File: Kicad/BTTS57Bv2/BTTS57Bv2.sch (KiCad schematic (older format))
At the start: 70 parts, among them K1-RES SW_Push, K2-Next SW_Push, K3-Mode SW_Push, K4-Valid SW_Push, P1 Conn_01x06, P2 Conn_01x04, P4 Conn_01x08, P5 Conn_01x02, U1 BNOR11, U2 A4950E, U3 EL-0631, U4 A4950E, U5 TLE5012B, U6 EL357NC, U7 STM32F103CBTx, U8 LD1117S33CTR, U9 PCA82C251, Y1 Crystal, p7 Conn_01x08

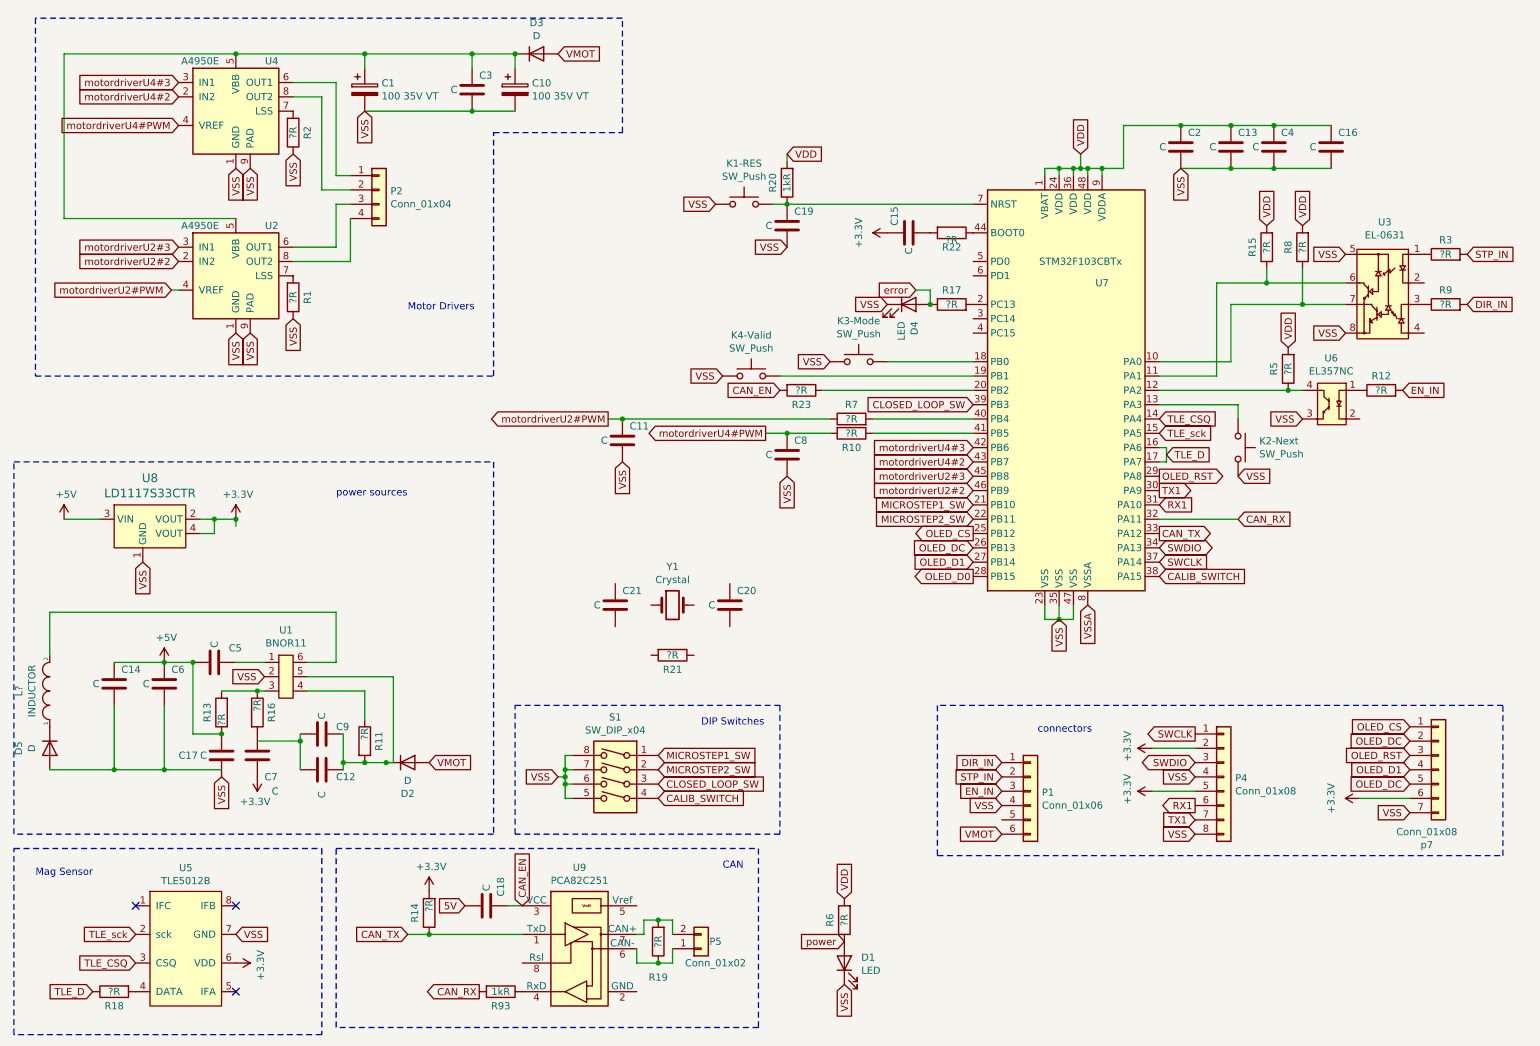
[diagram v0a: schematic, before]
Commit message: fix connection on CAN, add cristal wiring
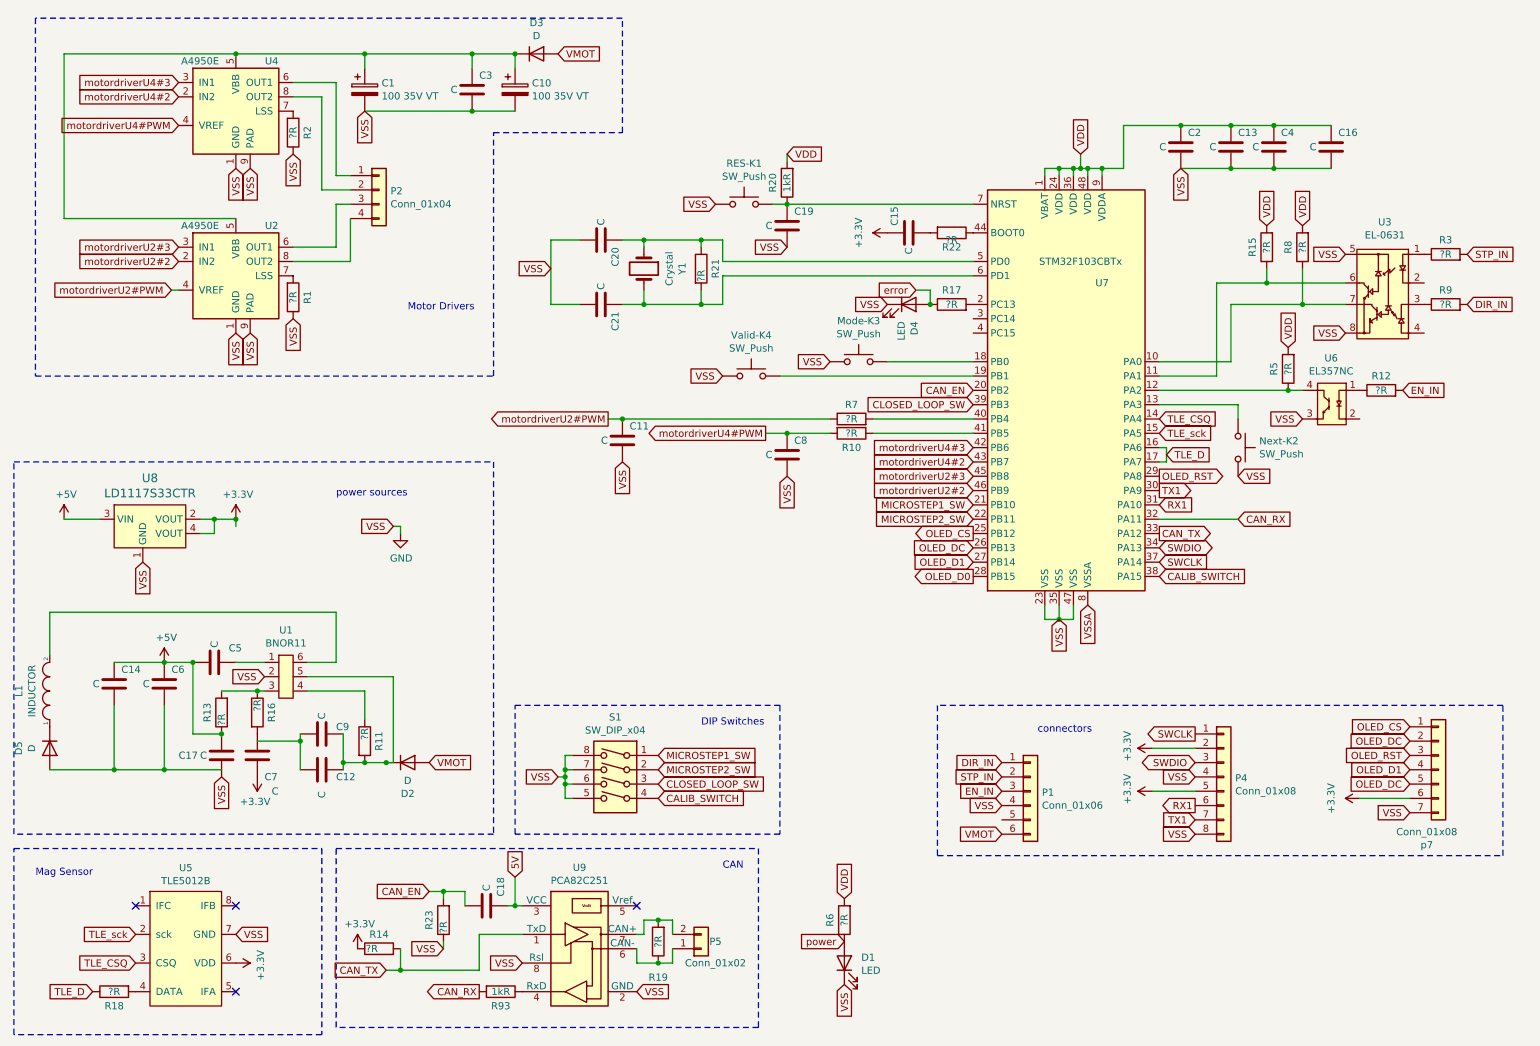
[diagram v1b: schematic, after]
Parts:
- gave numbers to parts that had none: 1
- renumbered K3-Mode to Mode-K3, K2-Next to Next-K2, K1-RES to RES-K1, K4-Valid to Valid-K4
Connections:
- net VSS is gone; now on net GND: C1.2, C10.2, C11.2, C13.2, C16.2, C17.2, C19.2, C2.2, C3.2, C4.2, C8.2, D1.1 (K), D4.1 (K), Mode-K3.1, Next-K2.2, P1.4 (Pin_4), P4.4 (Pin_4), P4.8 (Pin_8), R1.1, R2.1, RES-K1.1, S1.5, S1.6, S1.7, S1.8, U1.2, U2.1 (GND), U2.9 (PAD), U3.5, U3.8, U4.1 (GND), U4.9 (PAD), U5.7 (GND), U6.3, U7.23 (VSS), U7.35 (VSS), U7.47 (VSS), U8.1 (GND), Valid-K4.1, p7.7 (Pin_7)
- net +3V3: now also R14.1; no longer R14.2
- net 5V: now also C18.1, U9.3 (VCC); no longer C18.2
- net CAN_EN: now also C18.2, U7.20 (PB2); no longer C18.1, U9.3 (VCC)
- net CAN_TX: now also R14.2; no longer R14.1
- net GND: now reaches R23.1
- net GND: now also C20.2, C21.2, U9.2 (GND), U9.8 (Rsl); no longer U7.20 (PB2)
- net at U7.5 (PD0): now also C20.1, R21.1, Y1.1
- net at U7.6 (PD1): now also C21.1, R21.2, Y1.2
- no-connect marks 3 -> 4
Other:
- moved on the sheet: C20, C21, R14, R21, R23, Y1

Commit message: added footprint information changed orientation of oled connector added mounting holes PCB reverse creation (high parts are positionned according measurements, same for outline)
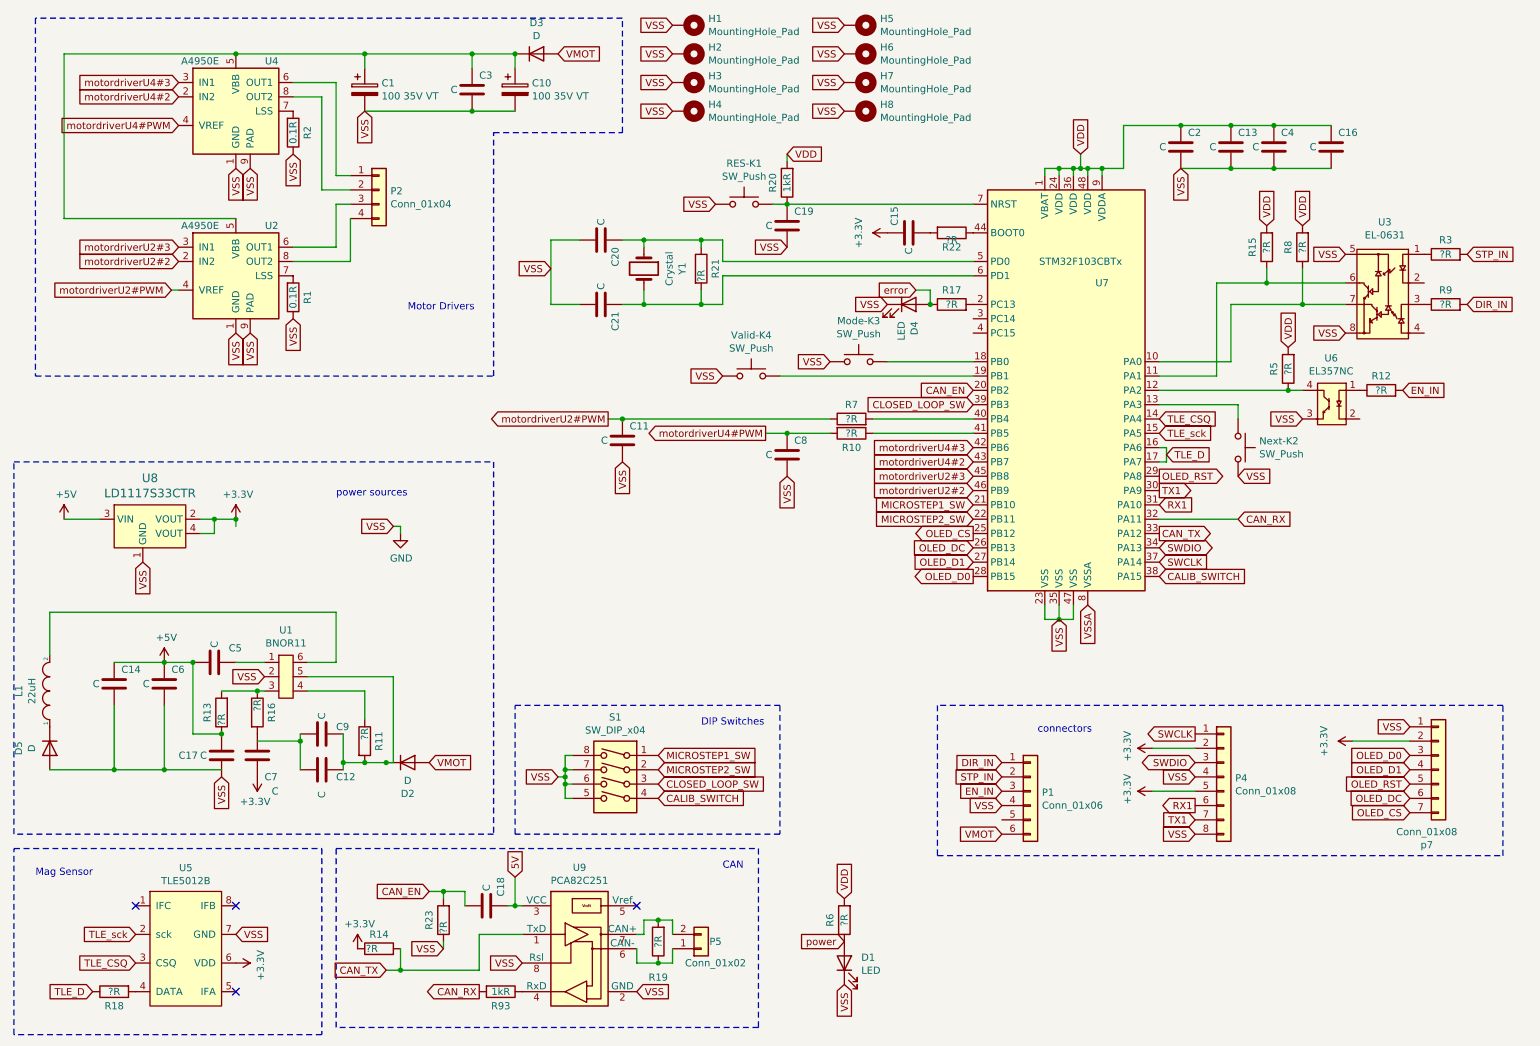
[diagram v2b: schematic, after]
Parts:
- added H1, H2, H3, H4, H5, H6, H7, H8: MountingHole_Pad, MountingHole:MountingHole_2.7mm_M2.5_ISO14580_Pad_TopBottom, symbol Mechanical:MountingHole_Pad
- C1, C10: footprint (none) -> Capacitor_SMD:CP_Elec_6.3x7.7
- C11, C12, C13, C14, C15, C16, C18, C19, C2, C20, C21, C4, C5, C8: footprint (none) -> Capacitor_SMD:C_0603_1608Metric
- C17, C3, C7: footprint (none) -> Capacitor_SMD:C_1812_4532Metric
- C6, C9: footprint (none) -> Capacitor_SMD:C_0805_2012Metric
- D1, D4: footprint (none) -> LED_SMD:LED_0603_1608Metric
- D2, D3, D5: footprint (none) -> Diode_SMD:D_2512_6332Metric
- L1: value INDUCTOR -> 22uH; footprint (none) -> Inductor_SMD:L_Wuerth_MAPI-4030; uncertain (none) -> yes
- Mode-K3, Next-K2, RES-K1, Valid-K4: footprint (none) -> Button_Switch_SMD:SW_Push_1P1T-SH_NO_CK_KMR2xxG
- P2: footprint (none) -> Connector_JST:JST_XH_B4B-XH-A_1x04_P2.50mm_Vertical
- P4: footprint (none) -> Connector_PinHeader_2.54mm:PinHeader_1x08_P2.54mm_Vertical
- R1, R2: value ?R -> 0.1R; footprint (none) -> Resistor_SMD:R_2512_6332Metric
- R10, R11, R13, R14, R15, R16, R17, R20, R21, R22, R23, R5, R6, R7, R8, R93: footprint (none) -> Resistor_SMD:R_0603_1608Metric
- R12, R18, R3, R9: footprint (none) -> Resistor_SMD:R_0805_2012Metric
- R19: footprint (none) -> Resistor_SMD:R_1206_3216Metric
- U3: footprint (none) -> Package_SO:SOP-8_3.9x4.9mm_P1.27mm
- U6: footprint (none) -> Package_SO:SOP-4_3.8x4.1mm_P2.54mm
- p7: footprint (none) -> Connector_PinSocket_2.54mm:PinSocket_1x07_P2.54mm_Vertical
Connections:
- net +3V3: now also p7.2 (Pin_2); no longer p7.6 (Pin_6)
- net GND: now also p7.1 (Pin_1), H1.1, H2.1, H3.1, H4.1, H5.1, H6.1, H7.1, H8.1; no longer p7.7 (Pin_7)
- net OLED_CS: now also p7.7 (Pin_7); no longer p7.1 (Pin_1)
- net OLED_D0: now also p7.3 (Pin_3)
- net OLED_DC: now also p7.6 (Pin_6); no longer p7.2 (Pin_2), p7.5 (Pin_5)
- net OLED_RST: now also p7.5 (Pin_5); no longer p7.3 (Pin_3)

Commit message: bug fix : wrong pin count order on optical tranceivers
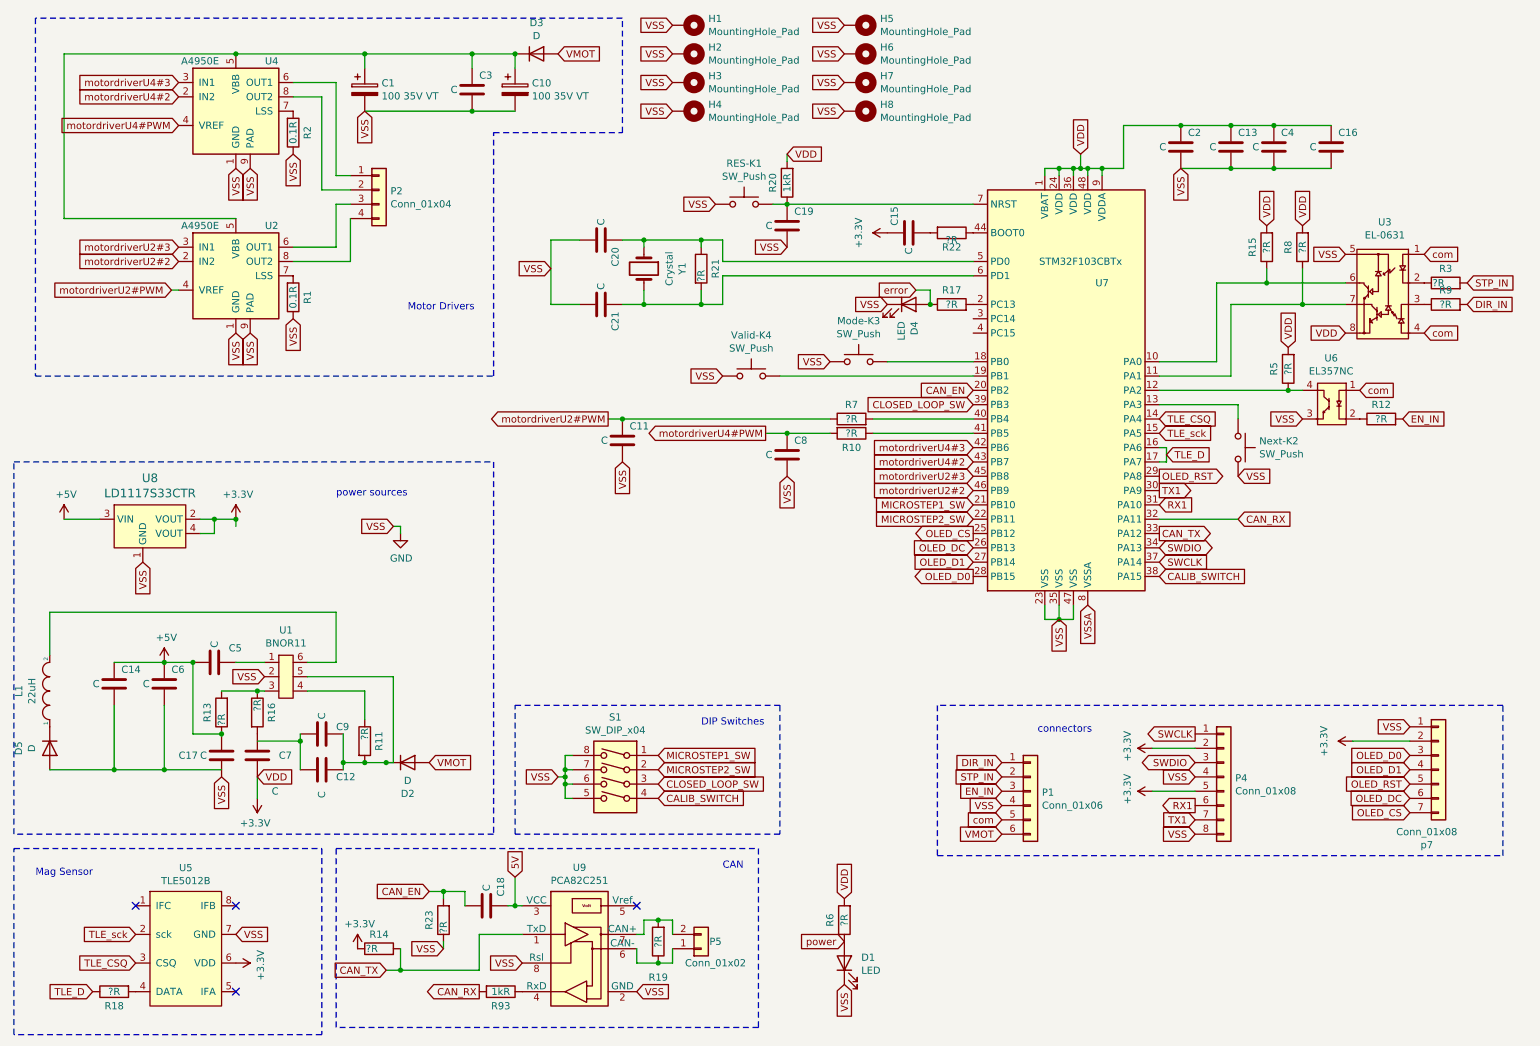
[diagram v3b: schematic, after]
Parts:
- C17, C3, C7: footprint Capacitor_SMD:C_1812_4532Metric -> Capacitor_SMD:C_0805_2012Metric
- U5: footprint (none) -> Package_SO:Infineon_PG-DSO-8-27_3.9x4.9mm_EP2.65x3mm
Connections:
- net VDD is gone; now on net +3V3: C13.1, C16.1, C2.1, C4.1, R15.2, R20.2, R5.2, R6.2, R8.2, U7.1 (VBAT), U7.24 (VDD), U7.36 (VDD), U7.48 (VDD), U7.9 (VDDA)
- net +3V3: now also U3.8
- net GND: no longer U3.8
- net at R8.1, U3.7: now also U7.11 (PA1); no longer U7.10 (PA0)
- net at R15.1, U3.6: now also U7.10 (PA0); no longer U7.11 (PA1)
- net at R3.1: now also U3.2; no longer U3.1
- net com: now reaches U3.4
- net com: now also P1.5 (Pin_5), U3.1, U6.1
- net at R12.1: now also U6.2; no longer U6.1
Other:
- moved on the sheet: R12, R3
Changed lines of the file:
@@
 Text GLabel 7300 4000 0    50   Input ~ 0
 MICROSTEP1_SW
-Text GLabel 10750 2250 2    50   Input ~ 0
+Text GLabel 10750 2450 2    50   Input ~ 0
 STP_IN
 Text GLabel 10750 2600 2    50   Input ~ 0
 DIR_IN
-Text GLabel 10300 3200 2    50   Input ~ 0
+Text GLabel 10300 3400 2    50   Input ~ 0
 EN_IN
 Text GLabel 7300 4200 0    50   Output ~ 0
@@
 L Device:R R12
 U 1 1 60AC6CB6
-P 10150 3200
-F 0 "R12" V 10250 3200 50  0000 C CNN
-F 1 "?R" V 10150 3200 50  0000 C CNN
-F 2 "Resistor_SMD:R_0805_2012Metric" V 10080 3200 50  0001 C CNN
-F 3 "~" H 10150 3200 50  0001 C CNN
-	1    10150 3200
+P 10150 3400
+F 0 "R12" V 10250 3400 50  0000 C CNN
+F 1 "?R" V 10150 3400 50  0000 C CNN
+F 2 "Resistor_SMD:R_0805_2012Metric" V 10080 3400 50  0001 C CNN
+F 3 "~" H 10150 3400 50  0001 C CNN
+	1    10150 3400
 	0    -1   -1   0
 $EndComp
@@
 L Device:R R3
 U 1 1 60AD1627
-P 10600 2250
-F 0 "R3" V 10700 2250 50  0000 C CNN
-F 1 "?R" V 10600 2250 50  0000 C CNN
-F 2 "Resistor_SMD:R_0805_2012Metric" V 10530 2250 50  0001 C CNN
-F 3 "~" H 10600 2250 50  0001 C CNN
-	1    10600 2250
+P 10600 2450
+F 0 "R3" V 10700 2450 50  0000 C CNN
+F 1 "?R" V 10600 2500 50  0000 C CNN
+F 2 "Resistor_SMD:R_0805_2012Metric" V 10530 2450 50  0001 C CNN
+F 3 "~" H 10600 2450 50  0001 C CNN
+	1    10600 2450
 	0    -1   -1   0
 $EndComp
@@
 Text GLabel 9600 2050 1    50   Input ~ 0
 VDD
-Wire Wire Line
-	9000 3100 8600 3100
 Text GLabel 9900 2250 0    50   Input ~ 0
-VSS
-Text GLabel 9900 2800 0    50   Input ~ 0
 VSS
 $Comp
@@
 	9350 2450 9900 2450
 Wire Wire Line
-	8600 3000 9100 3000
-Wire Wire Line
-	9000 3100 9000 2450
-Wire Wire Line
 	9000 2450 9350 2450
 Connection ~ 9350 2450
@@
 $EndComp
 Wire Wire Line
-	9100 2600 9100 3000
-Wire Wire Line
 	9100 2600 9600 2600
 Wire Wire Line
@@
 F 0 "C3" H 3850 1200 50  0000 L CNN
 F 1 "C" H 3650 1100 50  0000 L CNN
-F 2 "Capacitor_SMD:C_1812_4532Metric" H 3838 950 50  0001 C CNN
+F 2 "Capacitor_SMD:C_0805_2012Metric" H 3838 950 50  0001 C CNN
 F 3 "~" H 3800 1100 50  0001 C CNN
 	1    3800 1100
@@
 F 0 "U5" H 1800 8565 50  0000 C CNN
 F 1 "TLE5012B" H 1800 8474 50  0000 C CNN
-F 2 "" H 1850 7550 50  0001 C CNN
+F 2 "Package_SO:Infineon_PG-DSO-8-27_3.9x4.9mm_EP2.65x3mm" H 1850 7550 50  0001 C CNN
 F 3 "" H 1850 7550 50  0001 C CNN
 	1    1850 7550
@@
 F 0 "C17" H 1750 5750 50  0000 L CNN
 F 1 "C" H 1900 5750 50  0000 L CNN
-F 2 "Capacitor_SMD:C_1812_4532Metric" H 2088 5600 50  0001 C CNN
+F 2 "Capacitor_SMD:C_0805_2012Metric" H 2088 5600 50  0001 C CNN
 F 3 "~" H 2050 5750 50  0001 C CNN
 	1    2050 5750
@@
 U 1 1 60BACF1C
 P 2300 5750
-F 0 "C7" H 2350 5600 50  0000 L CNN
+F 0 "C7" H 2450 5750 50  0000 L CNN
 F 1 "C" H 2400 5500 50  0000 L CNN
-F 2 "Capacitor_SMD:C_1812_4532Metric" H 2338 5600 50  0001 C CNN
+F 2 "Capacitor_SMD:C_0805_2012Metric" H 2338 5600 50  0001 C CNN
 F 3 "~" H 2300 5750 50  0001 C CNN
 	1    2300 5750
@@
 L power:+3.3V #PWR0108
 U 1 1 60C37881
-P 2300 5900
-F 0 "#PWR0108" H 2300 5750 50  0001 C CNN
-F 1 "+3.3V" H 2315 6073 50  0000 C CNN
-F 2 "" H 2300 5900 50  0001 C CNN
-F 3 "" H 2300 5900 50  0001 C CNN
-	1    2300 5900
+P 2300 6050
+F 0 "#PWR0108" H 2300 5900 50  0001 C CNN
+F 1 "+3.3V" H 2315 6223 50  0000 C CNN
+F 2 "" H 2300 6050 50  0001 C CNN
+F 3 "" H 2300 6050 50  0001 C CNN
+	1    2300 6050
 	-1   0    0    1
 $EndComp
@@
 Text GLabel 6400 1250 0    50   Input ~ 0
 VSS
+Text GLabel 2300 5900 2    50   Input ~ 0
+VDD
+Wire Wire Line
+	2300 5900 2300 6050
+Wire Wire Line
+	9000 2450 9000 3000
+Wire Wire Line
+	9000 3000 8600 3000
+Wire Wire Line
+	9100 3100 8600 3100
+Wire Wire Line
+	9100 2600 9100 3100
+Text GLabel 9900 2800 0    50   Input ~ 0
+VDD
+Text GLabel 7500 6200 0    50   Input ~ 0
+com
+Text GLabel 10000 3200 2    50   Input ~ 0
+com
+Text GLabel 10450 2250 2    50   Input ~ 0
+com
+Text GLabel 10450 2800 2    50   Input ~ 0
+com
 $EndSCHEMATC
